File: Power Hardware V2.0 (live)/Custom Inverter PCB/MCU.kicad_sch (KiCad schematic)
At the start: 0 parts

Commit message: switches instead of relays. Short on half bridge fixed. encoder page made. root page connections fixed
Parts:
- added J4, J5: SSQ-110-03-G-D, SSQ_110_03_G_D (1):SAMTEC_SSQ-110-03-G-D, symbol SSQ-110-03-G-D:SSQ-110-03-G-D
- added U5: LAUNCHXL-F280049C, LAUNCHXL-F280049C:MODULE_LAUNCHXL-F280049C, symbol LAUNCHXL-F280049C:LAUNCHXL-F280049C
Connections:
- new net: U5.J2_16 (~{XRS}), U5.J6_56 (~{XRS})
- new net: U5.J11_10 (+3.3V), U5.J1_1 (+3.3V), U5.JP4_1 (+3.3V), U5.JP6_1 (+3.3V)
- new net: U5.J11_3 (GND_1), U5.J11_4 (GND_1), U5.J12_5 (GND_1), U5.J13_5 (GND_1), U5.J14_3 (GND_1), U5.J2_20 (GND_1), U5.J3_22 (GND_1), U5.J6_60 (GND_1), U5.J7_62 (GND_1)
- new net: U5.J11_9 (NC), U5.J1_5 (NC), U5.J2_17 (NC), U5.J2_18 (NC), U5.J5_49 (NC), U5.J5_50 (NC), U5.J6_57 (NC), U5.J6_58 (NC)
- new net: U5.J12_4 (+5V0), U5.J13_4 (+5V0), U5.J3_21 (+5V0), U5.JP5_1 (+5V0), U5.JP7_1 (+5V0)
- new net: U5.J15_2 (GND_2), U5.JP4_2 (GND_2), U5.JP4_3 (GND_2), U5.JP5_2 (GND_2), U5.JP5_3 (GND_2), U5.JP6_2 (GND_2), U5.JP6_3 (GND_2), U5.JP7_2 (GND_2), U5.JP7_3 (GND_2)
- new net +3.3V: J4.01
- new net GND: J4.04, J5.02
- new net INHA: J5.01
- new net INHB: J5.05
- new net INHC: J5.09
- new net INLA: J5.03
- new net INLB: J5.07
- new net INLC: J5.11
- new net ISENA: J4.18
- new net ISENB: J4.16
- new net ISENC: J4.14
- new net SEN_100V: J4.12
- new net VESNB: J4.08
- new net VSENA: J4.06
- new net VSENC: J4.10
- new net VSEN_12V: J4.20
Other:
- note added: "INTERFACE INPUTS"
- note added: "INTERFACE OUTPUTS"
- note added: "MCU CONNECTORS"

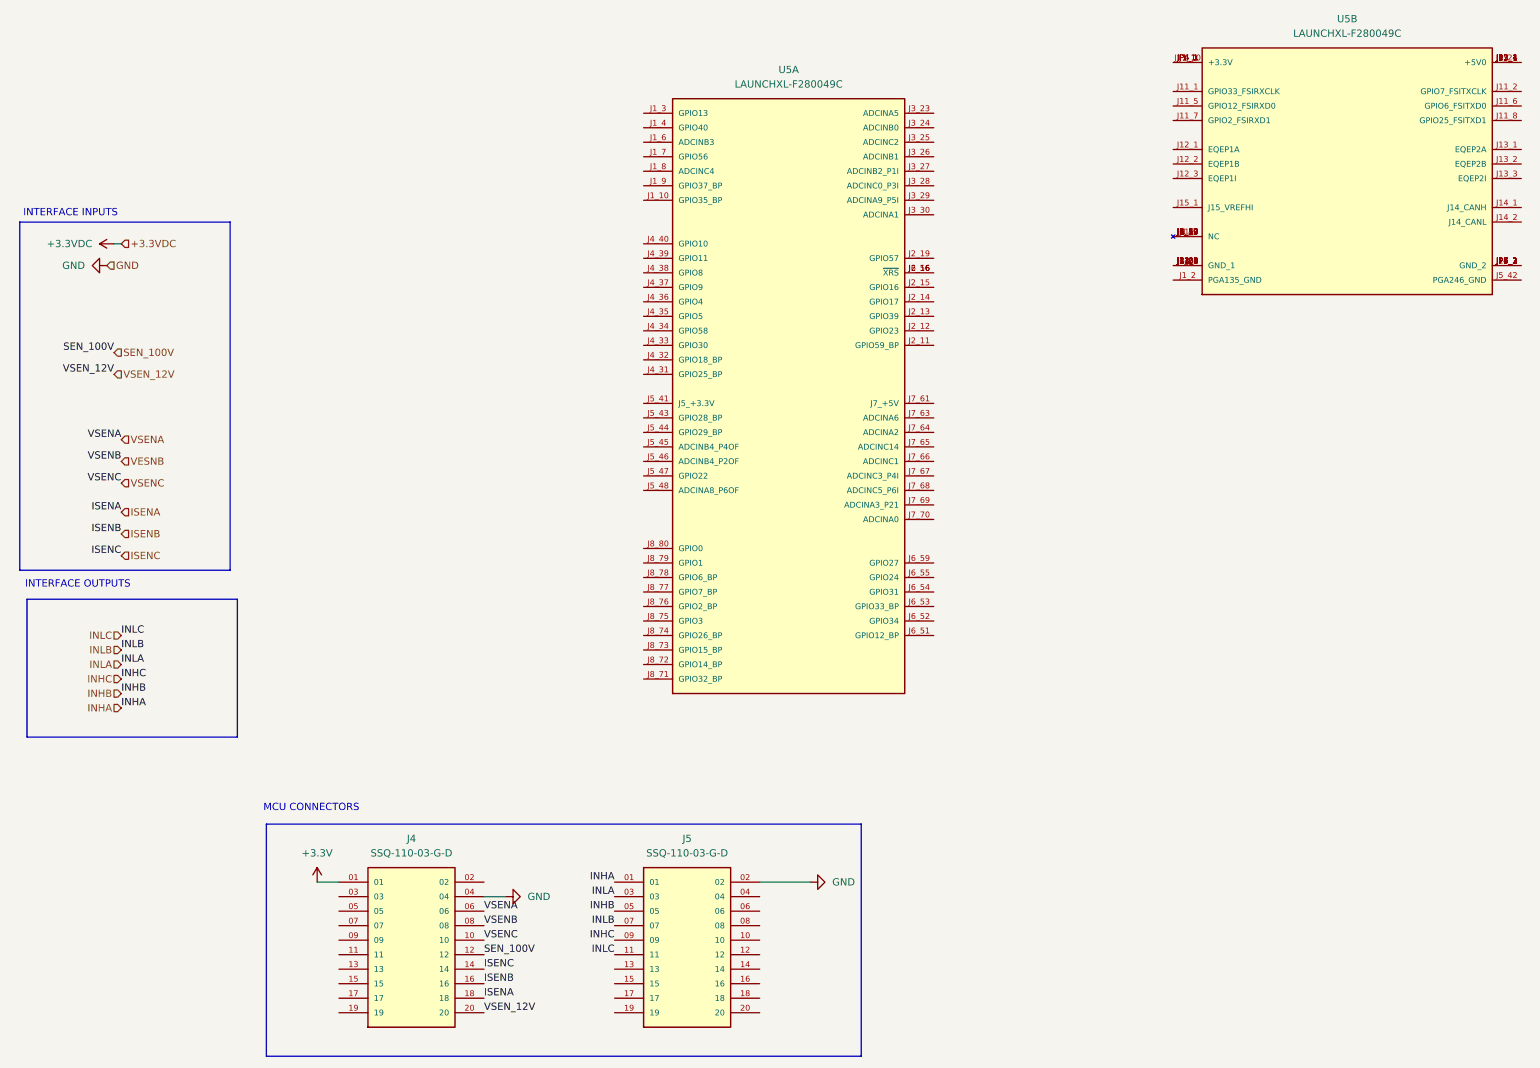
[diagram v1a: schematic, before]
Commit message: Schematic Changes
-Changed 3.3V regulator to a higher power unit for the sin-cos circuit (from 500mA to 3A)
-Fixed flipped MOTA,B,C connection to Output Terminal
- Current Sense IC setup
- Fuses for Phase current outputs
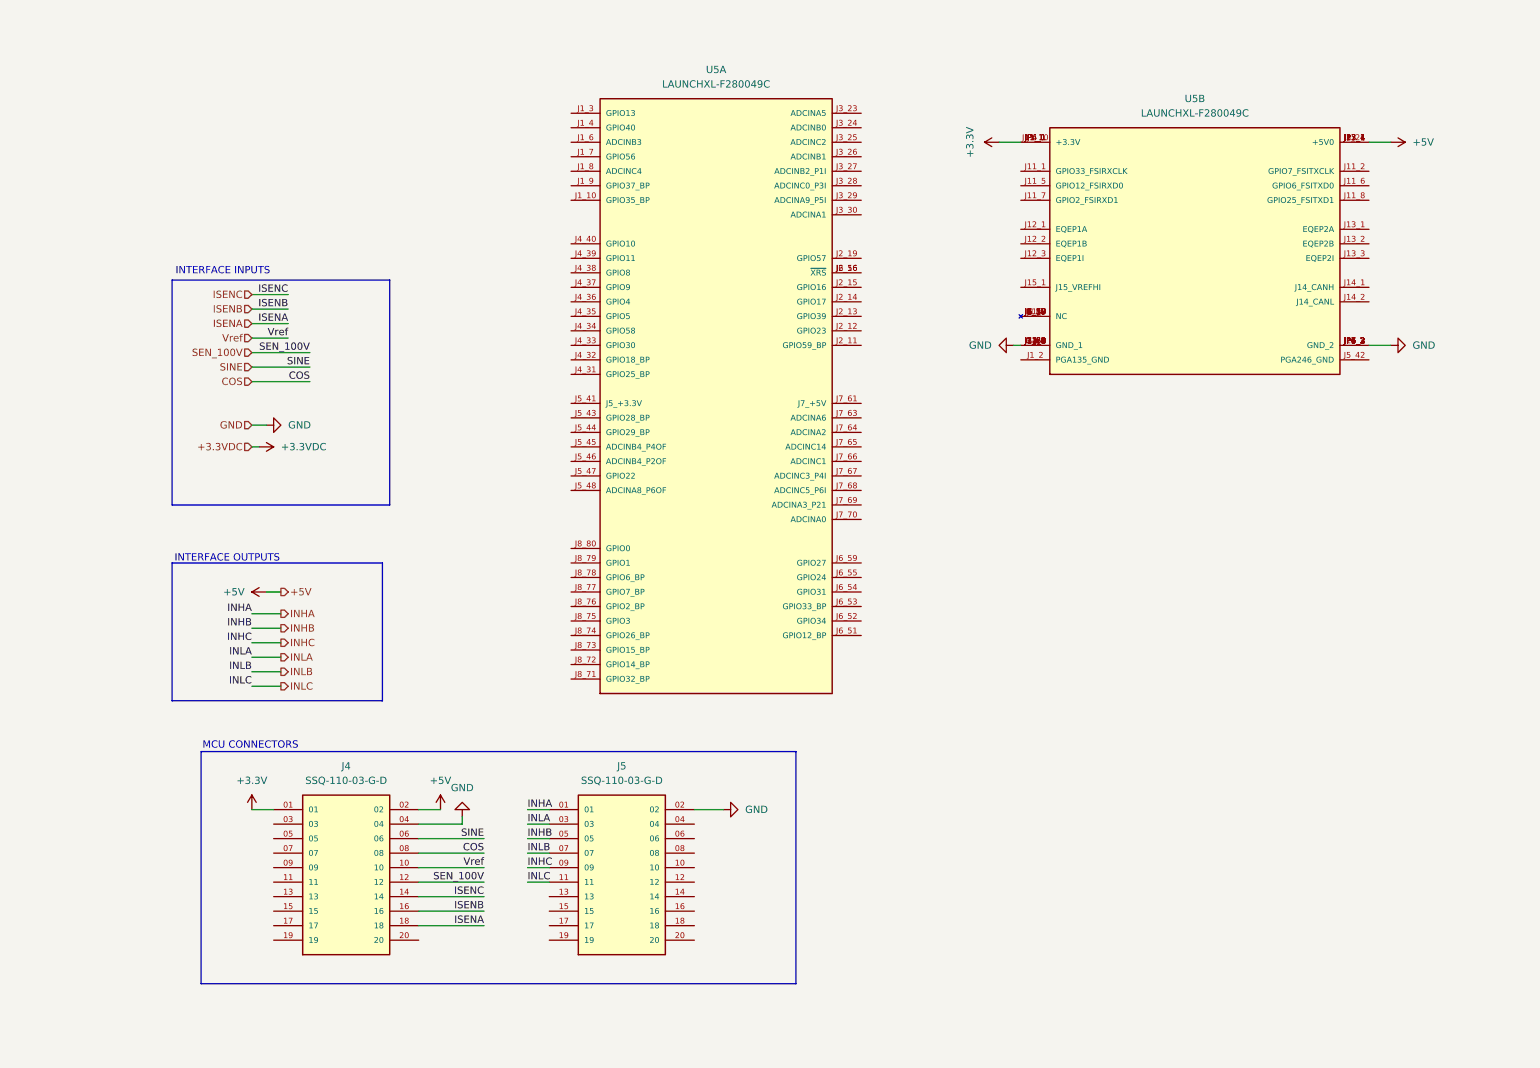
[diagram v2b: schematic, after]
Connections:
- net +3.3V: now also U5.J11_10 (+3.3V), U5.J1_1 (+3.3V), U5.JP4_1 (+3.3V), U5.JP6_1 (+3.3V)
- net GND: now also U5.J11_3 (GND_1), U5.J11_4 (GND_1), U5.J12_5 (GND_1), U5.J13_5 (GND_1), U5.J14_3 (GND_1), U5.J15_2 (GND_2), U5.J2_20 (GND_1), U5.J3_22 (GND_1), U5.J6_60 (GND_1), U5.J7_62 (GND_1), U5.JP4_2 (GND_2), U5.JP4_3 (GND_2), U5.JP5_2 (GND_2), U5.JP5_3 (GND_2), U5.JP6_2 (GND_2), U5.JP6_3 (GND_2), U5.JP7_2 (GND_2), U5.JP7_3 (GND_2)
- net +5V: now reaches J4.02
- net +5V: now also U5.J12_4 (+5V0), U5.J13_4 (+5V0), U5.J3_21 (+5V0), U5.JP5_1 (+5V0), U5.JP7_1 (+5V0)
- net VESNB renamed COS
- net VSENA renamed SINE
- net VSENC renamed Vref
- net VSEN_12V: no longer names the net of J4.20
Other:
- moved on the sheet: J4, J5, U5A, U5B

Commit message: footprint lib fixes
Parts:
- J4: value SSQ-110-03-G-D -> 0010897202; footprint SSQ_110_03_G_D (1):SAMTEC_SSQ-110-03-G-D -> (none); MANUFACTURER Samtec -> Molex; Part Number (none) -> 0010897202
- J5: value SSQ-110-03-G-D -> 0010897202; MANUFACTURER Samtec -> Molex; Part Number (none) -> 0010897202
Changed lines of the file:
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@@
 			)
 		)
-		(property "Value" "SSQ-110-03-G-D"
+		(property "Value" "0010897202"
 			(at 71.12 147.32 0)
 			(effects
@@
 			)
 		)
-		(property "Footprint" "SSQ_110_03_G_D (1):SAMTEC_SSQ-110-03-G-D"
+		(property "Footprint" ""
 			(at 71.12 165.1 0)
 			(effects
@@
 			)
 		)
-		(property "MANUFACTURER" "Samtec"
+		(property "MANUFACTURER" "Molex"
 			(at 71.12 165.1 0)
 			(effects
@@
 			)
 		)
-		(property "Part Number" ""
+		(property "Part Number" "0010897202"
 			(at 71.12 165.1 0)
 			(effects
@@
 			)
 		)
-		(property "Value" "SSQ-110-03-G-D"
+		(property "Value" "0010897202"
 			(at 119.38 147.32 0)
 			(effects
@@
 			)
 		)
-		(property "MANUFACTURER" "Samtec"
+		(property "MANUFACTURER" "Molex"
 			(at 119.38 165.1 0)
 			(effects
@@
 			)
 		)
-		(property "Part Number" ""
+		(property "Part Number" "0010897202"
 			(at 119.38 165.1 0)
 			(effects

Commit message: footprint fixes
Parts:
- removed J4: 0010897202, symbol SSQ-110-03-G-D:SSQ-110-03-G-D
- removed J5: 0010897202, SSQ_110_03_G_D (1):SAMTEC_SSQ-110-03-G-D, symbol SSQ-110-03-G-D:SSQ-110-03-G-D
- added J10, J4, J5, J9: 10897202, CONN20_0010897202_MOL, symbol 10897202:10897202
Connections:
- net COS: now also U5.J7_64 (ADCINA2)
- net INHA: now also U5.J8_80 (GPIO0)
- net INHB: now also U5.J8_78 (GPIO6_BP)
- net INHC: now also U5.J8_76 (GPIO2_BP)
- net INLA: now also U5.J8_79 (GPIO1)
- net INLB: now also U5.J8_77 (GPIO7_BP)
- net INLC: now also U5.J8_75 (GPIO3)
- net ISENA: now also U5.J7_67 (ADCINC3_P4I)
- net ISENB: now also U5.J7_68 (ADCINC5_P6I)
- net ISENC: now also U5.J7_69 (ADCINA3_P21)
- net SEN_100V: now also U5.J7_66 (ADCINC1)
- net SINE: now also U5.J7_63 (ADCINA6)
- net Vref: now also U5.J7_65 (ADCINC14)
